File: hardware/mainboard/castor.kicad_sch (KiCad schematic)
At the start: 46 parts, among them J7 OSC OUT, Q1 MMBT3906, U10 MCP6001-OT, U7 TL074, U8 TL074, U9 74LVC2G74

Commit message: exclude components from BOM
excluded:
- J11 (alternate USB connection)
- test points
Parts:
- TP11: now left out of the parts list
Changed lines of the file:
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@@
 		(unit 1)
 		(exclude_from_sim no)
-		(in_bom yes)
+		(in_bom no)
 		(on_board yes)
 		(dnp no)

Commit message: add alternate for TL074
added TL074CPWR as alternate in addition to TL074CPW
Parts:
- U8: MPN TL074CPW -> TL074CPW, TL074CPWR
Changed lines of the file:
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@@
 			)
 		)
-		(property "MPN" "TL074CPW"
+		(property "MPN" "TL074CPW, TL074CPWR"
 			(at 146.05 93.98 0)
 			(effects
@@
 			)
 		)
-		(property "MPN" "TL074CPW"
+		(property "MPN" "TL074CPW, TL074CPWR"
 			(at 223.52 56.515 0)
 			(effects
@@
 			)
 		)
-		(property "MPN" "TL074CPW"
+		(property "MPN" "TL074CPW, TL074CPWR"
 			(at 126.365 153.035 0)
 			(effects
@@
 			)
 		)
-		(property "MPN" "TL074CPW"
+		(property "MPN" "TL074CPW, TL074CPWR"
 			(at 250.825 146.05 0)
 			(effects

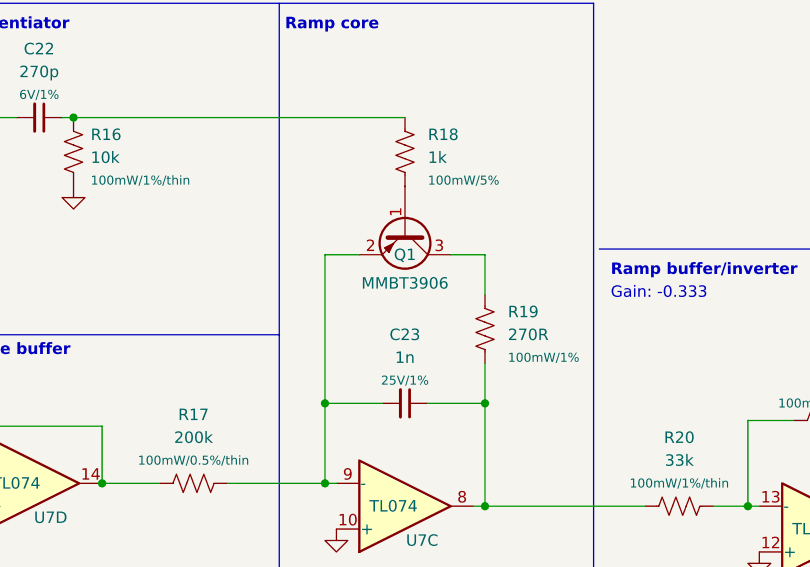
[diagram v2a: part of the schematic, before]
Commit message: add alternate for MMBT3906
alternate added CMPT3906G TR PBFREE
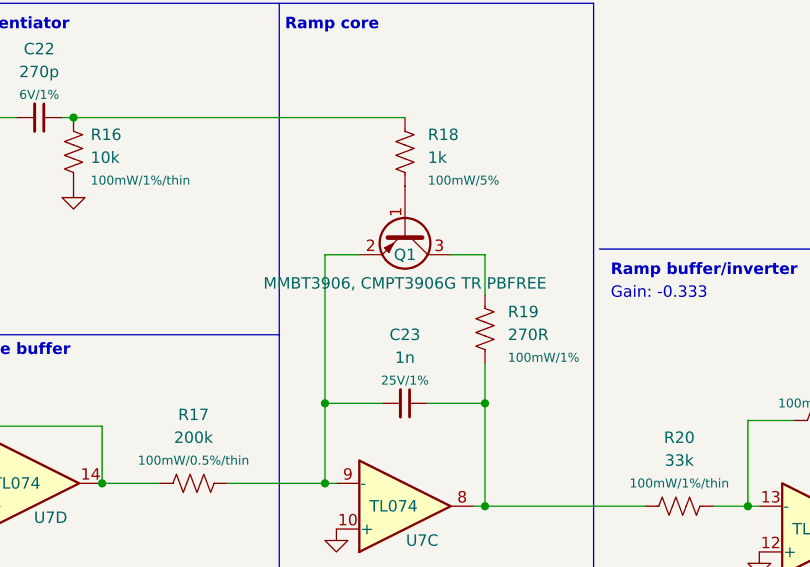
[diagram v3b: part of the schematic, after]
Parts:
- Q1: value MMBT3906 -> MMBT3906, CMPT3906G TR PBFREE
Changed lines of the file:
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@@
 			)
 		)
-		(property "Value" "MMBT3906"
+		(property "Value" "MMBT3906, CMPT3906G TR PBFREE"
 			(at 99.06 59.055 90)
 			(effects
